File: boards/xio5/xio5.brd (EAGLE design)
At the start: 170 x 170 mm, 89 parts, among them IC1 PCAL6416APW,118, J1 98424-G52-14ALF

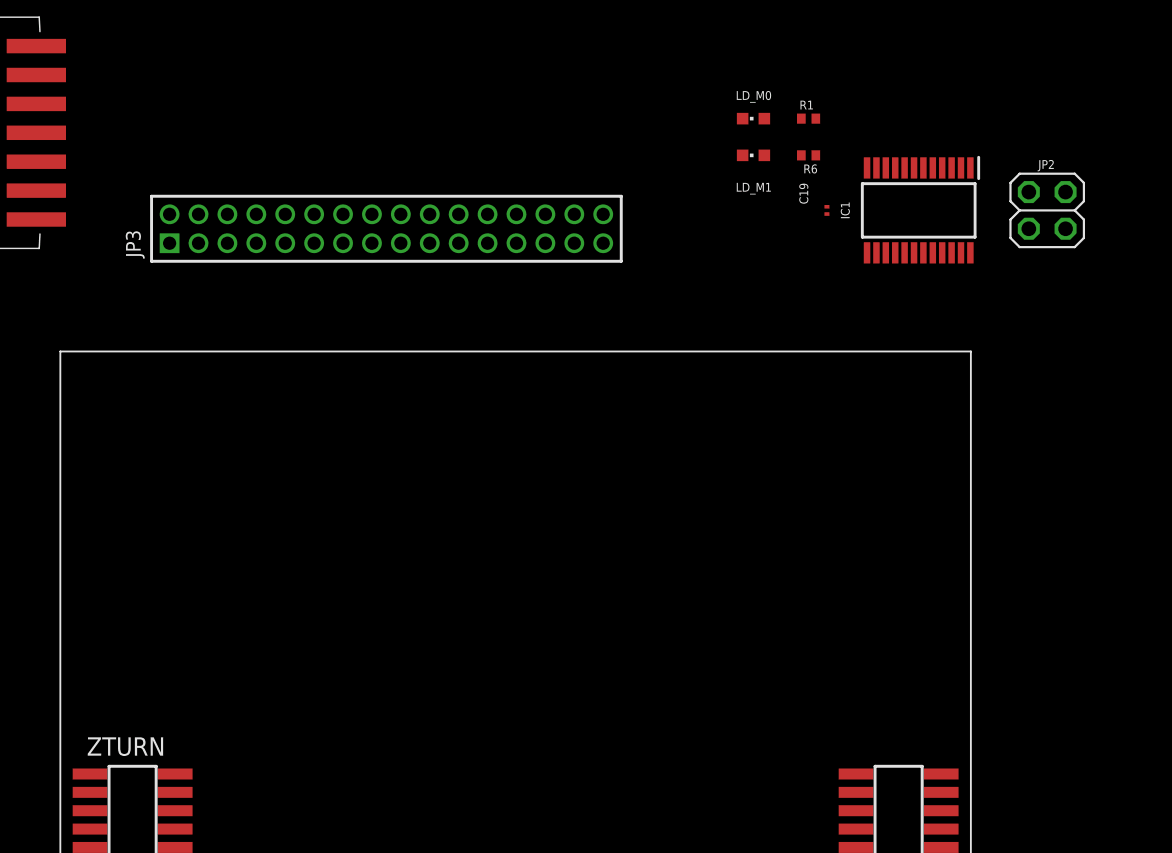
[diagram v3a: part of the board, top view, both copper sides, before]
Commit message: Correct the SPI interface bugs
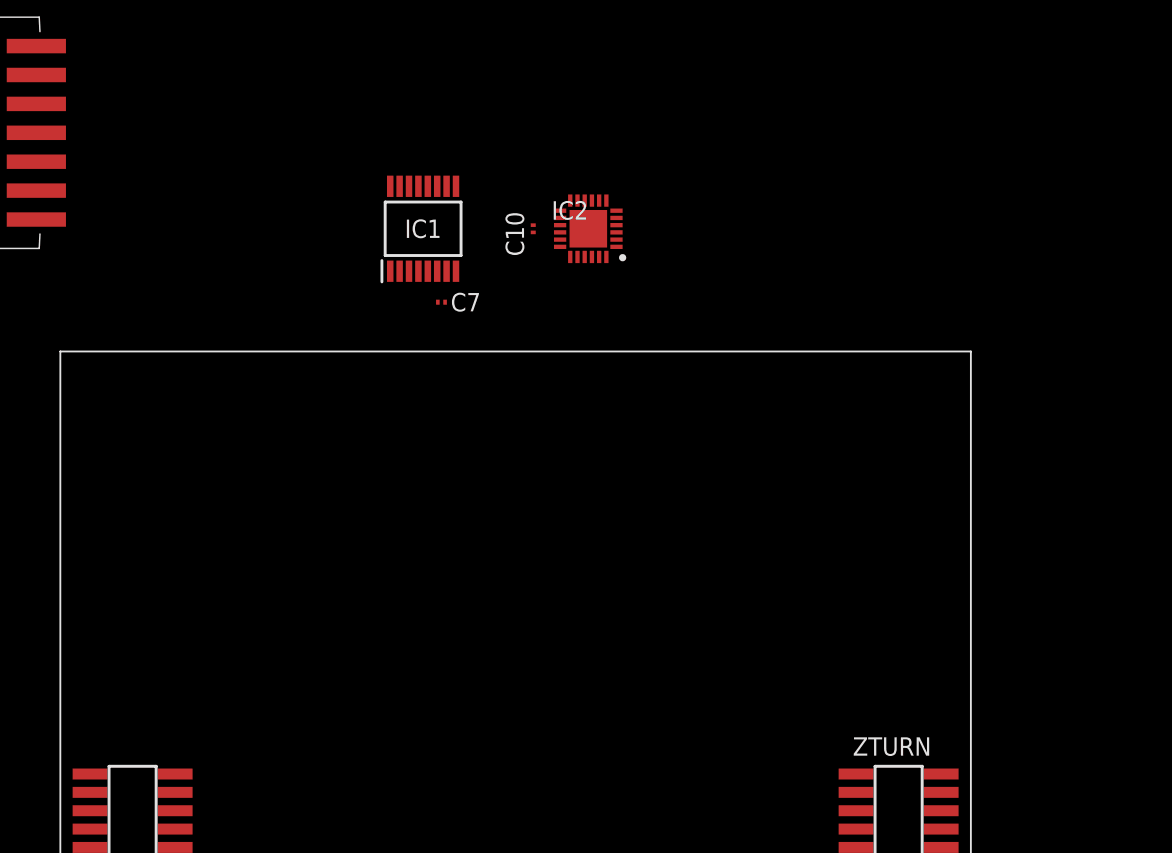
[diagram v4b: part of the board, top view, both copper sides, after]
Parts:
- removed C19: 0.1uF, rcl:C0201
- removed JP2: (no value), pinhead:2X02
- removed JP3: (no value), pinhead-2:2X16M
- removed LD_M0, LD_M1: Orange, led:CHIPLED_0603
- removed R1, R6: 59R, rcl:R0402
- added C10, C7: 0.1uF, rcl:C0201
- added IC2: XRA1405IL24-F, samacsys:QFN50P400X400X100-25N
- IC1: value PCAL6416APW,118 -> TC74LCX138FT; device samacsys:SOP65P640X110-24N -> samacsys:SOP65P640X120-16N
- moved IC1 34.3 mm to (36.8, 110.5), turned to 90 degrees
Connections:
- removed net HSPI0_IRQ0: SLOT0.A7, ZTURN.CN2_74
- removed net HSPI0_IRQ1: SLOT1.A7, ZTURN.CN2_72
- removed net HSPI0_IRQ2: SLOT2.A7, ZTURN.CN2_68
- removed net HSPI0_MISO: SLOT0.A4, SLOT1.A4, SLOT2.A4, ZTURN.CN2_78
- removed net HSPI0_MOSI: SLOT0.A5, SLOT1.A5, SLOT2.A5, ZTURN.CN2_76
- removed net HSPI0_SS0: SLOT0.A6, ZTURN.CN2_66
- removed net HSPI0_SS1: SLOT1.A6, ZTURN.CN2_64
- removed net HSPI0_SS2: SLOT2.A6, ZTURN.CN2_62
- removed net HSPI1_IRQ0: SLOT3.A7, ZTURN.CN2_54
- removed net HSPI1_IRQ1: SLOT4.A7, ZTURN.CN2_52
- removed net HSPI1_IRQ2: ZTURN.CN2_48
- removed net HSPI1_MISO: SLOT3.A4, SLOT4.A4, ZTURN.CN2_58
- removed net HSPI1_MOSI: SLOT3.A5, SLOT4.A5, ZTURN.CN2_56
- removed net HSPI1_SS0: SLOT3.A6, ZTURN.CN2_46
- removed net HSPI1_SS1: SLOT4.A6, ZTURN.CN2_44
- removed net HSPI1_SS2: ZTURN.CN2_42
- removed net N$2: IC1.11, R6.2
- removed net N$7: IC1.10, R1.2
- removed net N$8: LD_M0.A, R1.1
- removed net SCL: IC1.22, JP2.2, ZTURN.CN1_78
- removed net SDA: IC1.23, JP2.4, ZTURN.CN1_76
- removed net SX_PRESENT: IC1.9, JP3.11
- removed net XIO0: IC1.13, JP3.13
- removed net XIO1: IC1.14, JP3.15
- removed net XIO2: IC1.15, JP3.17
- removed net XIO3: IC1.16, JP3.19
- removed net XIO4: IC1.17, JP3.21
- removed net XIO5: IC1.18, JP3.23
- removed net XIO6: IC1.19, JP3.25
- removed net XIO7: IC1.20, JP3.27
- removed net XSPI_IRQ: JP3.5, ZTURN.CN2_28
- removed net XSPI_MISO: JP2.1, JP3.7, ZTURN.CN2_32
- removed net XSPI_MOSI: JP2.3, JP3.9, ZTURN.CN2_34
- new net S5_PRESENT: IC2.17
- new net SPI1_CLK: SLOT0.A4, SLOT1.A4, SLOT2.A4, SLOT3.A4, SLOT4.A4, ZTURN.CN2_72
- new net SPI1_MISO: SLOT0.A5, SLOT1.A5, SLOT2.A5, SLOT3.A5, SLOT4.A5, ZTURN.CN2_68
- new net SPI1_MOSI: SLOT0.A6, SLOT1.A6, SLOT2.A6, SLOT3.A6, SLOT4.A6, ZTURN.CN2_66
- new net SPI2_CLK: IC2.19, ZTURN.CN2_58
- new net SPI2_CS0: IC2.18, ZTURN.CN2_64
- new net SPI2_CS1: ZTURN.CN2_62
- new net SPI2_IRQ: IC2.22, ZTURN.CN2_52
- new net SPI2_MISO: IC2.20, ZTURN.CN2_56
- new net SPI2_MOSI: IC2.24, ZTURN.CN2_54
- new net SPI_IRQ0: IC2.1, SLOT0.A8
- new net SPI_IRQ1: IC2.2, SLOT1.A8
- new net SPI_IRQ2: IC2.3, SLOT2.A8
- new net SPI_IRQ3: IC2.4, SLOT3.A8
- new net SPI_IRQ4: IC2.5, SLOT4.A8
- new net SPI_IRQ5: IC2.6
- new net SPI_SS0: IC1.15, SLOT0.A7
- new net SPI_SS1: IC1.14, SLOT1.A7
- new net SPI_SS2: IC1.13, SLOT2.A7
- new net SPI_SS3: IC1.12, SLOT3.A7
- new net SPI_SS4: IC1.11, SLOT4.A7
- new net SPI_SS5: IC1.10
- new net SPI_SS6: IC1.9
- new net SPI_SS7: IC1.7
- net +3V3: now also C10.1, C7.1, IC1.16, IC1.6, IC2.21, IC2.23; no longer C19.1, IC1.2, IC1.24
- net +5V: no longer JP3.1, JP3.3
- net GND: now also C10.2, C7.2, IC1.4, IC1.5, IC1.8, IC2.25, IC2.9; no longer C19.2, IC1.12, IC1.21, JP3.29, JP3.31, LD_M0.C, LD_M1.C, SLOT0.A8, SLOT1.A8, SLOT2.A8, SLOT3.A8, SLOT4.A8
- net N$3: now also IC1.1, ZTURN.CN2_74; no longer LD_M1.A, R6.1
- net N$4: now also IC1.2, ZTURN.CN2_76; no longer IC1.1, ZTURN.CN2_36
- net N$5: now also ZTURN.CN2_78; no longer ZTURN.CN2_38
- net S0_PRESENT: now also IC2.12; no longer IC1.4
- net S1_PRESENT: now also IC2.13; no longer IC1.5
- net S2_PRESENT: now also IC2.14; no longer IC1.6
- net S3_PRESENT: now also IC2.15; no longer IC1.7
- net S4_PRESENT: now also IC2.16; no longer IC1.8
- net ZBUS0: no longer JP3.32
- net ZBUS1: no longer JP3.30
- net ZBUS10: no longer JP3.12
- net ZBUS11: no longer JP3.10
- net ZBUS12: no longer JP3.8
- net ZBUS13: no longer JP3.6
- net ZBUS14: no longer JP3.4
- net ZBUS15: no longer JP3.2
- net ZBUS2: no longer JP3.28
- net ZBUS3: no longer JP3.26
- net ZBUS4: no longer JP3.24
- net ZBUS5: no longer JP3.22
- net ZBUS6: no longer JP3.20
- net ZBUS7: no longer JP3.18
- net ZBUS8: no longer JP3.16
- net ZBUS9: no longer JP3.14

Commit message: First pass at a ready-to-go board. Now to debug
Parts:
- added JP2: (no value), pinhead-2:2X20M
- added JP3: (no value), pinhead-2:2X10M
- added JP4, JP5: (no value), pinhead-2:2X04M
- added R1, R6: 22R, rcl:R0201
- added U$1: MPBI+, pbxl:2X25
- moved C10 75.5 mm to (99.1, 58.4)
- moved IC1 75.5 mm to (91.4, 58.4)
- moved IC2 75.5 mm to (102.9, 58.4)
- moved C7 75.5 mm to (92.7, 53.3)
- moved C13 8.03 mm to (140.2, 130.9)
- moved C15 8.03 mm to (144.0, 116.9)
- moved C16 8.03 mm to (145.3, 144.9)
- moved C17 8.03 mm to (140.2, 144.9)
- moved C18 8.03 mm to (145.6, 130.6)
- moved C3 8.03 mm to (140.2, 116.9)
- moved LVL_AHI 8.03 mm to (142.7, 139.8)
- moved LVL_ALO 8.03 mm to (142.7, 111.9)
- moved LVL_D 8.03 mm to (142.7, 125.8)
- moved R25 8.03 mm to (138.9, 130.9)
- moved R26 8.03 mm to (138.9, 144.9)
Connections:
- new net I2C0_SCL: JP2.37, JP3.4, ZTURN.CN1_78
- new net I2C0_SDA: JP2.35, JP3.2, ZTURN.CN1_76
- new net N$10: R1.1, ZTURN.CN2_72
- new net N$11: R6.1, ZTURN.CN2_58
- new net N$2: JP3.10, ZTURN.CN1_71
- new net N$6: JP3.12, ZTURN.CN1_75
- new net N$7: JP3.14, ZTURN.CN1_73
- new net N$8: JP3.16, ZTURN.CN1_74
- new net N$9: JP3.18, ZTURN.CN1_72
- new net S6_PRESENT: IC2.16, JP4.5
- new net S7_PRESENT: IC2.17, JP5.5
- new net SPI_IRQ6: IC2.7, JP4.3
- new net SPI_IRQ7: IC2.8, JP5.3
- new net XBUS0: JP2.26, JP3.13, ZTURN.CN2_28
- new net XBUS1: JP2.28, JP3.15, ZTURN.CN2_32
- new net XBUS2: JP2.30, JP3.17, ZTURN.CN2_34
- new net XBUS3: JP2.32, JP3.19, ZTURN.CN2_36
- new net XBUS4: JP2.34, ZTURN.CN2_38
- new net XBUS5: JP2.36, ZTURN.CN2_42
- new net XBUS6: JP2.38, ZTURN.CN2_44
- new net XBUS7: JP2.40, ZTURN.CN2_46
- new net XBUS8: ZTURN.CN2_48
- net !HI_CCTL!: now also U$1.30
- net !HI_EXTSEL!: now also U$1.26
- net !HI_HALT!: now also U$1.33
- net !HI_IRQ!: now also U$1.23
- net !HI_MPD!: now also U$1.25
- net !HI_RST!: now also U$1.31
- net !HI_S4!: now also U$1.37
- net !HI_S5!: now also U$1.39
- net +3V3: now also JP2.6, JP2.8, JP3.5, JP3.7
- net +5V: now also JP2.2, JP2.4, JP3.1, JP3.3, JP4.1, JP5.1, U$1.17, U$1.41
- net GND: now also JP2.24, JP2.33, JP2.39, JP3.11, JP3.20, JP3.6, JP3.8, JP3.9, JP4.7, JP4.8, JP5.7, JP5.8, U$1.18, U$1.35
- net HI_A0: now also U$1.16
- net HI_A1: now also U$1.14
- net HI_A10: now also U$1.46
- net HI_A11: now also U$1.44
- net HI_A12: now also U$1.42
- net HI_A13: now also U$1.40
- net HI_A14: now also U$1.38
- net HI_A15: now also U$1.36
- net HI_A2: now also U$1.12
- net HI_A3: now also U$1.10
- net HI_A4: now also U$1.8
- net HI_A5: now also U$1.6
- net HI_A6: now also U$1.4
- net HI_A7: now also U$1.2
- net HI_A8: now also U$1.50
- net HI_A9: now also U$1.48
- net HI_CLK: now also U$1.29
- net HI_D0: now also U$1.15
- net HI_D1: now also U$1.13
- net HI_D2: now also U$1.11
- net HI_D3: now also U$1.9
- net HI_D4: now also U$1.7
- net HI_D5: now also U$1.5
- net HI_D6: now also U$1.3
- net HI_D7: now also U$1.1
- net HI_R/!W!: now also U$1.27
- net HI_RD4: now also U$1.43
- net HI_RD5: now also U$1.45
- net S0_PRESENT: now also IC2.10; no longer IC2.12
- net S1_PRESENT: now also IC2.11; no longer IC2.13
- net S2_PRESENT: now also IC2.12; no longer IC2.14
- net S3_PRESENT: now also IC2.13; no longer IC2.15
- net S4_PRESENT: now also IC2.14; no longer IC2.16
- net S5_PRESENT: now also IC2.15, JP2.20; no longer IC2.17
- net SPI1_CLK: now also JP4.2, JP5.2, R1.2; no longer ZTURN.CN2_72
- net SPI1_MISO: now also JP4.4, JP5.4
- net SPI1_MOSI: now also JP4.6, JP5.6
- net SPI2_CLK: now also JP2.10, R6.2; no longer ZTURN.CN2_58
- net SPI2_CS1: now also JP2.12
- net SPI2_IRQ: now also JP2.16
- net SPI2_MISO: now also JP2.14
- net SPI2_MOSI: now also JP2.18
- net SPI_IRQ5: now also JP2.22
- net ZBUS0: now also JP2.31
- net ZBUS1: now also JP2.29
- net ZBUS10: now also JP2.11
- net ZBUS11: now also JP2.9
- net ZBUS12: now also JP2.7
- net ZBUS13: now also JP2.5
- net ZBUS14: now also JP2.3
- net ZBUS15: now also JP2.1
- net ZBUS2: now also JP2.27
- net ZBUS3: now also JP2.25
- net ZBUS4: now also JP2.23
- net ZBUS5: now also JP2.21
- net ZBUS6: now also JP2.19
- net ZBUS7: now also JP2.17
- net ZBUS8: now also JP2.15
- net ZBUS9: now also JP2.13
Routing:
- net GND: track 0.00 -> 703.2 mm, vias 0 -> 21
- net +3V3: track 0.00 -> 608.6 mm, vias 0 -> 22
- net SPI1_MISO: track 0.00 -> 280.4 mm, vias 0 -> 3
- net SPI1_MOSI: track 0.00 -> 271.4 mm, vias 0 -> 2
- net SPI1_CLK: track 0.00 -> 268.0 mm, vias 0 -> 2
- net !LO_IRQ!: track 0.00 -> 267.3 mm, vias 0 -> 4
- net LO_A10: track 0.00 -> 264.2 mm, vias 0 -> 8
- net LO_D0: track 0.00 -> 261.5 mm, vias 0 -> 4
- net LO_D1: track 0.00 -> 258.9 mm, vias 0 -> 3
- net LO_R/!W!: track 0.00 -> 256.8 mm, vias 0 -> 3
- net LO_A8: track 0.00 -> 253.3 mm, vias 0 -> 4
- net LO_A12: track 0.00 -> 249.7 mm, vias 0 -> 6
- net LO_D6: track 0.00 -> 247.4 mm, vias 0 -> 4
- net +5V: track 0.00 -> 243.6 mm, vias 2 -> 10
- net ZBUS3: track 0.00 -> 236.6 mm, vias 0 -> 5
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- added copper zone on layer 15, net +5V
- added copper zone on layer 2, net GND
- removed copper zone on layer 15, net GND
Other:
- board text added: "Xio -5- © 2019 SjG"
- board text removed: "Top board - Zturn Lite Middle - B2B, Cartridge, SAS & HDMI underneath Base - PCIe x5, Dips All SMT parts are 1206"
- board text removed: "Xio -3- © 2019 SjG"

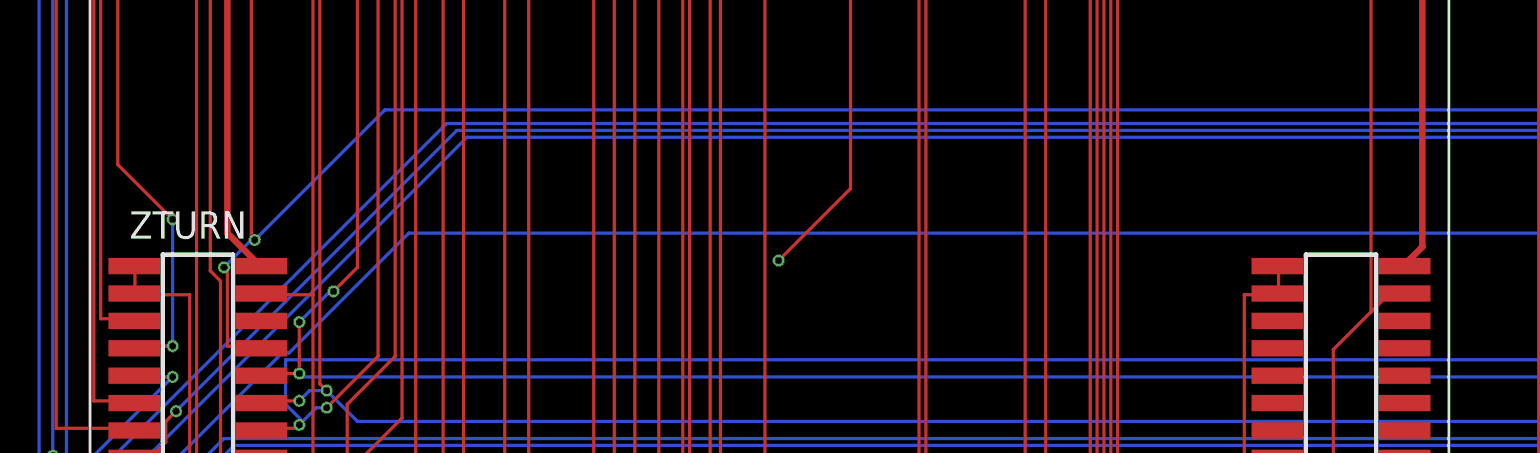
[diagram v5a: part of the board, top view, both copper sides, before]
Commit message: Start the process of verifying the schematic
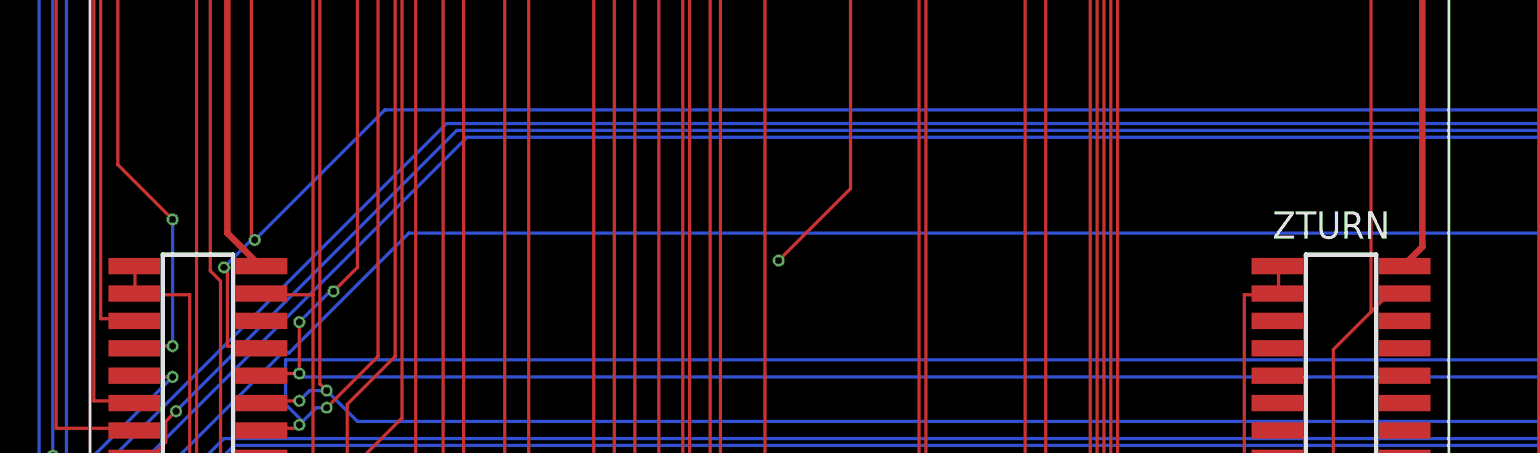
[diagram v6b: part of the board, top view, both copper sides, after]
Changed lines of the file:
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@@
 <drawing>
 <settings>
-<setting alwaysvectorfont="no"/>
+<setting alwaysvectorfont="yes"/>
 <setting verticaltext="up"/>
 </settings>
-<grid distance="10" unitdist="mm" unit="mm" style="lines" multiple="1" display="yes" altdistance="1" altunitdist="mil" altunit="mil"/>
+<grid distance="0.05" unitdist="inch" unit="inch" style="lines" multiple="1" display="yes" altdistance="1" altunitdist="mil" altunit="mil"/>
 <layers>
 <layer number="1" name="Top" color="4" fill="1" visible="yes" active="yes"/>
@@
 </element>
 <element name="ZTURN" library="pbxl" package="ZTURN" value="ZTURN" x="43.73" y="48" smashed="yes">
-<attribute name="NAME" x="66.555" y="74.035" size="1.27" layer="25"/>
 <attribute name="NAME" x="12.73" y="1" size="1.27" layer="21"/>
 <attribute name="NAME" x="13.555" y="74.035" size="1.27" layer="25"/>
+<attribute name="NAME" x="66.555" y="74.035" size="1.27" layer="25"/>
 <attribute name="VALUE" x="71.035" y="44.19" size="1.27" layer="27" rot="R90"/>
 </element>
@@
 <element name="U$1" library="pbxl" package="2X25" value="MPBI+" x="115.57" y="158.75" smashed="yes" rot="R90">
 <attribute name="NAME" x="80.645" y="155.575" size="1.27" layer="25" ratio="10" rot="R90"/>
+<attribute name="NOSTUFF" value="1" x="115.57" y="158.75" size="1.778" layer="27" rot="R90" display="off"/>
 <attribute name="VALUE" x="120.015" y="127" size="1.27" layer="27" rot="R90"/>
 </element>
@@
 <via x="140.81125" y="107.95" extent="1-16" drill="0.3"/>
 <via x="135.89" y="73.9775" extent="1-16" drill="0.3"/>
-<wire x1="138.89" y1="41.26" x2="121.11" y2="41.26" width="0" layer="19" extent="1-1"/>
+<wire x1="163.1" y1="87.94" x2="166.1" y2="87.94" width="0" layer="19" extent="1-1"/>
+<wire x1="159.6" y1="87.94" x2="163.1" y2="87.94" width="0" layer="19" extent="1-1"/>
+<wire x1="163.1" y1="70.14" x2="163.1" y2="87.94" width="0" layer="19" extent="1-1"/>
+<wire x1="165.1" y1="70.14" x2="163.1" y2="70.14" width="0" layer="19" extent="1-1"/>
+<wire x1="159.6" y1="70.14" x2="163.1" y2="70.14" width="0" layer="19" extent="1-1"/>
+<wire x1="140.2525" y1="84.995" x2="140.955" y2="83.07" width="0" layer="19" extent="1-1"/>
+<wire x1="145.6478" y1="128.105" x2="145.6478" y2="122.255" width="0" layer="19" extent="1-1"/>
+<wire x1="113.49" y1="145.78" x2="128.27" y2="157.48" width="0" layer="19" extent="1-1"/>
+<wire x1="113.49" y1="143.78" x2="113.49" y2="145.78" width="0" layer="19" extent="1-1"/>
+<wire x1="105.41" y1="160.02" x2="113.49" y2="145.78" width="0" layer="19" extent="1-1"/>
+<wire x1="86.82" y1="145.78" x2="105.41" y2="160.02" width="0" layer="19" extent="1-1"/>
+<wire x1="86.82" y1="143.78" x2="86.82" y2="145.78" width="0" layer="19" extent="1-1"/>
+<wire x1="156.67" y1="41.26" x2="159.6" y2="70.14" width="0" layer="19" extent="1-1"/>
+<wire x1="138.89" y1="41.26" x2="156.67" y2="41.26" width="0" layer="19" extent="1-1"/>
+<wire x1="121.11" y1="41.26" x2="138.89" y2="41.26" width="0" layer="19" extent="1-1"/>
+<wire x1="103.33" y1="41.26" x2="121.11" y2="41.26" width="0" layer="19" extent="1-1"/>
+<wire x1="92.96" y1="53.34" x2="103.33" y2="41.26" width="0" layer="19" extent="1-1"/>
+<wire x1="98.83" y1="8.26" x2="96.83" y2="9.26" width="0" layer="19" extent="1-1"/>
+<wire x1="66.78" y1="48.635" x2="72.68" y2="47.365" width="0" layer="19" extent="1-1"/>
+<wire x1="81.05" y1="10.26" x2="79.05" y2="9.26" width="0" layer="19" extent="1-1"/>
+<wire x1="81.05" y1="8.26" x2="81.05" y2="10.26" width="0" layer="19" extent="1-1"/>
+<wire x1="79.05" y1="17.26" x2="81.05" y2="10.26" width="0" layer="19" extent="1-1"/>
+<wire x1="96.83" y1="17.26" x2="96.83" y2="9.26" width="0" layer="19" extent="1-1"/>
+<wire x1="116.61" y1="10.26" x2="107.625" y2="9.54" width="0" layer="19" extent="1-1"/>
+<wire x1="116.61" y1="8.26" x2="116.61" y2="10.26" width="0" layer="19" extent="1-1"/>
+<wire x1="114.61" y1="17.26" x2="116.61" y2="10.26" width="0" layer="19" extent="1-1"/>
+<wire x1="134.39" y1="8.26" x2="125.405" y2="9.54" width="0" layer="19" extent="1-1"/>
+<wire x1="141.915" y1="9.535" x2="134.39" y2="8.26" width="0" layer="19" extent="1-1"/>
+<wire x1="152.17" y1="10.26" x2="150.17" y2="9.26" width="0" layer="19" extent="1-1"/>
+<wire x1="150.17" y1="17.26" x2="152.17" y2="10.26" width="0" layer="19" extent="1-1"/>
+<wire x1="132.39" y1="17.26" x2="134.39" y2="8.26" width="0" layer="19" extent="1-1"/>
+<wire x1="85.55" y1="41.26" x2="92.96" y2="53.34" width="0" layer="19" extent="1-1"/>
+<wire x1="82.28" y1="114.22" x2="86.82" y2="143.78" width="0" layer="19" extent="1-1"/>
+<wire x1="82.28" y1="112.22" x2="82.28" y2="114.22" width="0" layer="19" extent="1-1"/>
+<wire x1="80.28" y1="110.22" x2="82.28" y2="112.22" width="0" layer="19" extent="1-1"/>
+<wire x1="80.28" y1="108.22" x2="80.28" y2="110.22" width="0" layer="19" extent="1-1"/>
+<wire x1="82.28" y1="100.22" x2="80.28" y2="108.22" width="0" layer="19" extent="1-1"/>
+<wire x1="57.1" y1="106.95" x2="80.28" y2="108.22" width="0" layer="19" extent="1-1"/>
+<wire x1="51.1" y1="106.95" x2="57.1" y2="106.95" width="0" layer="19" extent="1-1"/>
+<wire x1="41.1" y1="108.95" x2="51.1" y2="106.95" width="0" layer="19" extent="1-1"/>
+<wire x1="4.47" y1="111.13" x2="41.1" y2="108.95" width="0" layer="19" extent="1-1"/>
 </signal>
 <signal name="+3V3" class="9">
